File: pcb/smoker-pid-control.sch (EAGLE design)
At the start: 16 parts, among them Q1 IRLIZ44N, SW1 EC12E_SW

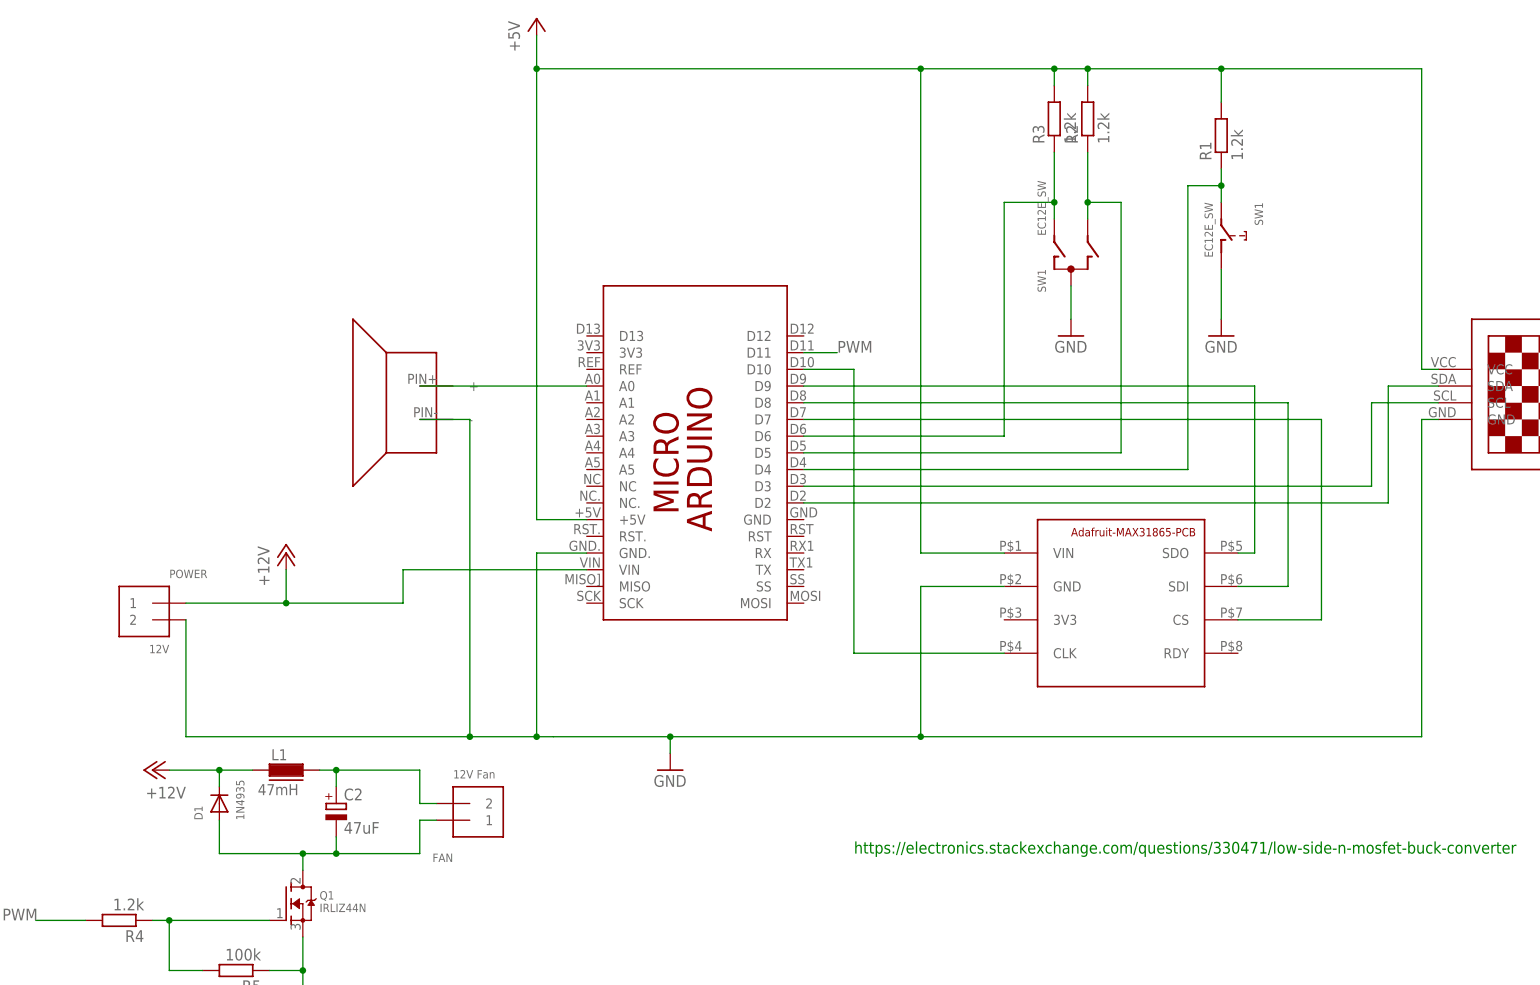
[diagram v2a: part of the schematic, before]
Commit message: single layer Layout, groundplane fix, stronger airwires
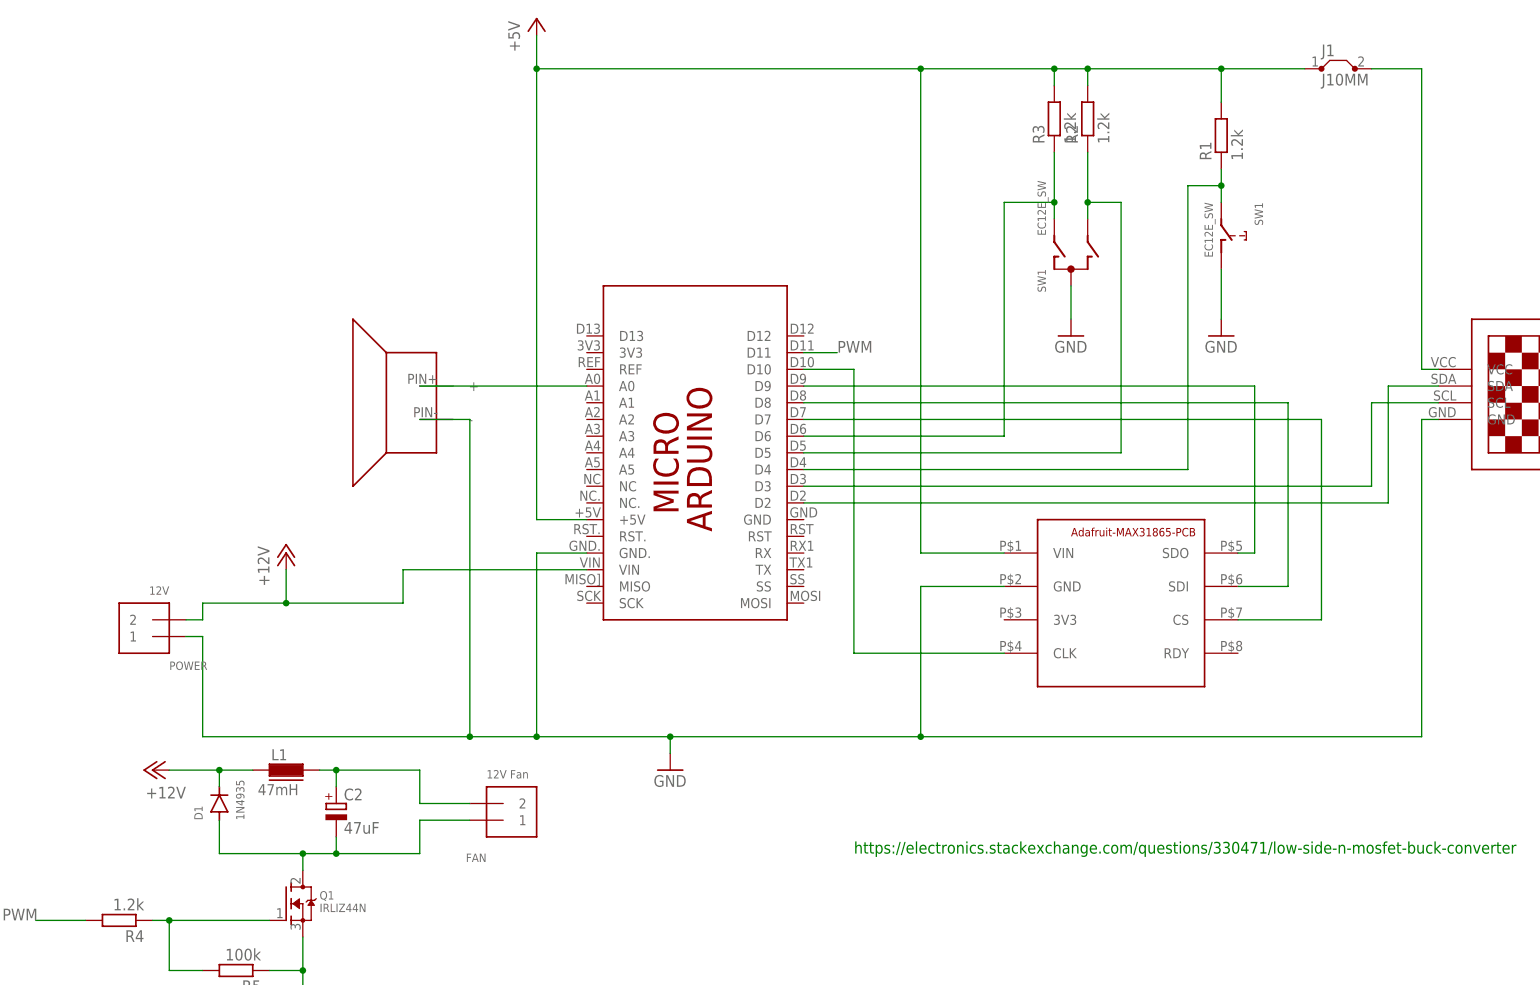
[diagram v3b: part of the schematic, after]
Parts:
- added J1: J10MM, jumper:J10MM
- D1: device adafruit:DIODEDO-1N4148 -> diode:DIODE-DO34-7
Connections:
- new net N$13: J1.2, U$2.VCC
- net +12V: now also POWER.2; no longer POWER.1
- net +5V: now also J1.1; no longer U$2.VCC
- net GND: now also POWER.1; no longer POWER.2
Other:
- moved on the sheet: FAN, POWER
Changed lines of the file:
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@@
 <layers>
 <layer number="1" name="Top" color="4" fill="1" visible="no" active="no"/>
+<layer number="2" name="Route2" color="1" fill="3" visible="no" active="no"/>
+<layer number="3" name="Route3" color="4" fill="3" visible="no" active="no"/>
+<layer number="4" name="Route4" color="1" fill="4" visible="no" active="no"/>
+<layer number="5" name="Route5" color="4" fill="4" visible="no" active="no"/>
+<layer number="6" name="Route6" color="1" fill="8" visible="no" active="no"/>
+<layer number="7" name="Route7" color="4" fill="8" visible="no" active="no"/>
+<layer number="8" name="Route8" color="1" fill="2" visible="no" active="no"/>
+<layer number="9" name="Route9" color="4" fill="2" visible="no" active="no"/>
+<layer number="10" name="Route10" color="1" fill="7" visible="no" active="no"/>
+<layer number="11" name="Route11" color="4" fill="7" visible="no" active="no"/>
+<layer number="12" name="Route12" color="1" fill="5" visible="no" active="no"/>
+<layer number="13" name="Route13" color="4" fill="5" visible="no" active="no"/>
+<layer number="14" name="Route14" color="1" fill="6" visible="no" active="no"/>
+<layer number="15" name="Route15" color="4" fill="6" visible="no" active="no"/>
 <layer number="16" name="Bottom" color="1" fill="1" visible="no" active="no"/>
 <layer number="17" name="Pads" color="2" fill="1" visible="no" active="no"/>
@@
 <part name="Q1" library="adafruit" library_urn="urn:adsk.eagle:library:420" deviceset="MOSFET-N" device="GDS_TO220V" package3d_urn="urn:adsk.eagle:package:6240882/1" value="IRLIZ44N"/>
 <part name="L1" library="_fastron_07HCP" deviceset="07HCP-*" device="" technology="100U" value="47mH"/>
-<part name="D1" library="adafruit" library_urn="urn:adsk.eagle:library:420" deviceset="DIODE" device="DO-1N4148" package3d_urn="urn:adsk.eagle:package:6240748/1" value="1N4935"/>
+<part name="D1" library="diode" library_urn="urn:adsk.eagle:library:210" deviceset="DIODE-" device="DO34-7" package3d_urn="urn:adsk.eagle:package:43348/1" value="1N4935"/>
 <part name="C2" library="rcl" library_urn="urn:adsk.eagle:library:334" deviceset="CPOL-EU" device="E5-8.5" package3d_urn="urn:adsk.eagle:package:23374/1" value="47uF"/>
 <part name="P+3" library="supply1" library_urn="urn:adsk.eagle:library:371" deviceset="+12V" device=""/>
@@
 <part name="R4" library="rcl" library_urn="urn:adsk.eagle:library:334" deviceset="R-EU_" device="0207/10" package3d_urn="urn:adsk.eagle:package:23491/2" value="1.2k"/>
 <part name="R5" library="rcl" library_urn="urn:adsk.eagle:library:334" deviceset="R-EU_" device="0207/10" package3d_urn="urn:adsk.eagle:package:23491/2" value="100k"/>
+<part name="J1" library="jumper" library_urn="urn:adsk.eagle:library:252" deviceset="J" device="10MM" package3d_urn="urn:adsk.eagle:package:15468/1"/>
 </parts>
 <sheets>
@@
 <attribute name="VALUE" x="193.04" y="208.28" size="1.27" layer="96" rot="R270"/>
 </instance>
-<instance part="POWER" gate="G$1" x="33.02" y="144.78" smashed="yes" rot="MR0">
-<attribute name="VALUE" x="35.56" y="139.7" size="1.27" layer="96" rot="MR0"/>
-<attribute name="NAME" x="35.56" y="152.4" size="1.27" layer="95" rot="MR180"/>
-</instance>
-<instance part="FAN" gate="G$1" x="81.28" y="116.84" smashed="yes" rot="MR180">
-<attribute name="VALUE" x="78.74" y="121.92" size="1.27" layer="96" rot="MR180"/>
-<attribute name="NAME" x="78.74" y="109.22" size="1.27" layer="95" rot="R180"/>
+<instance part="POWER" gate="G$1" x="33.02" y="144.78" smashed="yes" rot="R180">
+<attribute name="VALUE" x="35.56" y="149.86" size="1.27" layer="96" rot="R180"/>
+<attribute name="NAME" x="35.56" y="137.16" size="1.27" layer="95"/>
+</instance>
+<instance part="FAN" gate="G$1" x="86.36" y="116.84" smashed="yes" rot="MR180">
+<attribute name="VALUE" x="83.82" y="121.92" size="1.27" layer="96" rot="MR180"/>
+<attribute name="NAME" x="83.82" y="109.22" size="1.27" layer="95" rot="R180"/>
 </instance>
 <instance part="GND1" gate="1" x="111.76" y="121.92" smashed="yes">
@@
 <attribute name="NAME" x="49.53" y="89.9414" size="1.778" layer="95" rot="R180"/>
 <attribute name="VALUE" x="49.53" y="94.742" size="1.778" layer="96" rot="R180"/>
+</instance>
+<instance part="J1" gate="1" x="213.36" y="228.6" smashed="yes">
+<attribute name="NAME" x="210.82" y="230.505" size="1.778" layer="95"/>
+<attribute name="VALUE" x="210.82" y="226.06" size="1.778" layer="96"/>
 </instance>
 </instances>
@@
 <net name="+12V" class="0">
 <segment>
-<pinref part="POWER" gate="G$1" pin="1"/>
-<wire x1="38.1" y1="147.32" x2="53.34" y2="147.32" width="0.1524" layer="91"/>
 <wire x1="53.34" y1="147.32" x2="71.12" y2="147.32" width="0.1524" layer="91"/>
 <wire x1="71.12" y1="147.32" x2="71.12" y2="152.4" width="0.1524" layer="91"/>
@@
 <pinref part="P+1" gate="1" pin="+12V"/>
 <wire x1="53.34" y1="152.4" x2="53.34" y2="147.32" width="0.1524" layer="91"/>
+<pinref part="POWER" gate="G$1" pin="2"/>
+<wire x1="38.1" y1="144.78" x2="40.64" y2="144.78" width="0.1524" layer="91"/>
+<wire x1="40.64" y1="144.78" x2="40.64" y2="147.32" width="0.1524" layer="91"/>
+<wire x1="40.64" y1="147.32" x2="53.34" y2="147.32" width="0.1524" layer="91"/>
 <junction x="53.34" y="147.32"/>
 </segment>
@@
 <segment>
 <wire x1="81.28" y1="127" x2="91.44" y2="127" width="0.1524" layer="91"/>
-<wire x1="93.98" y1="127" x2="111.76" y2="127" width="0.1524" layer="91"/>
+<wire x1="91.44" y1="127" x2="111.76" y2="127" width="0.1524" layer="91"/>
 <wire x1="111.76" y1="127" x2="149.86" y2="127" width="0.1524" layer="91"/>
 <wire x1="149.86" y1="127" x2="226.06" y2="127" width="0.1524" layer="91"/>
@@
 <wire x1="228.6" y1="175.26" x2="226.06" y2="175.26" width="0.1524" layer="91"/>
 <wire x1="226.06" y1="175.26" x2="226.06" y2="127" width="0.1524" layer="91"/>
-<wire x1="38.1" y1="127" x2="81.28" y2="127" width="0.1524" layer="91"/>
-<wire x1="38.1" y1="127" x2="38.1" y2="144.78" width="0.1524" layer="91"/>
-<pinref part="POWER" gate="G$1" pin="2"/>
 <pinref part="GND1" gate="1" pin="GND"/>
+<wire x1="40.64" y1="127" x2="81.28" y2="127" width="0.1524" layer="91"/>
 <wire x1="111.76" y1="124.46" x2="111.76" y2="127" width="0.1524" layer="91"/>
 <junction x="111.76" y="127"/>
@@
 <wire x1="99.06" y1="154.94" x2="91.44" y2="154.94" width="0.1524" layer="91"/>
 <wire x1="91.44" y1="154.94" x2="91.44" y2="127" width="0.1524" layer="91"/>
-<wire x1="91.44" y1="127" x2="93.98" y2="127" width="0.1524" layer="91"/>
 <junction x="91.44" y="127"/>
+<pinref part="POWER" gate="G$1" pin="1"/>
+<wire x1="38.1" y1="142.24" x2="40.64" y2="142.24" width="0.1524" layer="91"/>
+<wire x1="40.64" y1="142.24" x2="40.64" y2="127" width="0.1524" layer="91"/>
 </segment>
 <segment>
@@
 <wire x1="170.18" y1="228.6" x2="175.26" y2="228.6" width="0.1524" layer="91"/>
 <wire x1="175.26" y1="228.6" x2="195.58" y2="228.6" width="0.1524" layer="91"/>
-<wire x1="195.58" y1="228.6" x2="226.06" y2="228.6" width="0.1524" layer="91"/>
-<wire x1="226.06" y1="228.6" x2="226.06" y2="182.88" width="0.1524" layer="91"/>
-<pinref part="U$2" gate="G$1" pin="VCC"/>
-<wire x1="226.06" y1="182.88" x2="228.6" y2="182.88" width="0.1524" layer="91"/>
 <pinref part="U$1" gate="G$1" pin="VIN"/>
 <wire x1="162.56" y1="154.94" x2="149.86" y2="154.94" width="0.1524" layer="91"/>
@@
 <pinref part="R1" gate="G$1" pin="2"/>
 <wire x1="195.58" y1="223.52" x2="195.58" y2="228.6" width="0.1524" layer="91"/>
-<junction x="195.58" y="228.6"/>
 <pinref part="R2" gate="G$1" pin="2"/>
 <wire x1="175.26" y1="226.06" x2="175.26" y2="228.6" width="0.1524" layer="91"/>
@@
 <wire x1="170.18" y1="226.06" x2="170.18" y2="228.6" width="0.1524" layer="91"/>
 <junction x="170.18" y="228.6"/>
+<pinref part="J1" gate="1" pin="1"/>
+<wire x1="208.28" y1="228.6" x2="195.58" y2="228.6" width="0.1524" layer="91"/>
+<junction x="195.58" y="228.6"/>
 </segment>
 </net>
@@
 <wire x1="73.66" y1="121.92" x2="73.66" y2="116.84" width="0.1524" layer="91"/>
 <pinref part="FAN" gate="G$1" pin="2"/>
-<wire x1="73.66" y1="116.84" x2="76.2" y2="116.84" width="0.1524" layer="91"/>
+<wire x1="73.66" y1="116.84" x2="81.28" y2="116.84" width="0.1524" layer="91"/>
 </segment>
 </net>
@@
 <segment>
 <pinref part="D1" gate="G$1" pin="A"/>
-<pinref part="FAN" gate="G$1" pin="1"/>
 <wire x1="43.18" y1="109.22" x2="43.18" y2="114.3" width="0.1524" layer="91"/>
-<wire x1="76.2" y1="114.3" x2="73.66" y2="114.3" width="0.1524" layer="91"/>
 <wire x1="73.66" y1="114.3" x2="73.66" y2="109.22" width="0.1524" layer="91"/>
 <wire x1="73.66" y1="109.22" x2="60.96" y2="109.22" width="0.1524" layer="91"/>
@@
 <wire x1="55.88" y1="106.68" x2="55.88" y2="109.22" width="0.1524" layer="91"/>
 <junction x="55.88" y="109.22"/>
+<pinref part="FAN" gate="G$1" pin="1"/>
+<wire x1="81.28" y1="114.3" x2="73.66" y2="114.3" width="0.1524" layer="91"/>
 </segment>
 </net>
@@
 </segment>
 </net>
+<net name="N$13" class="0">
+<segment>
+<pinref part="U$2" gate="G$1" pin="VCC"/>
+<wire x1="226.06" y1="228.6" x2="226.06" y2="182.88" width="0.1524" layer="91"/>
+<wire x1="226.06" y1="182.88" x2="228.6" y2="182.88" width="0.1524" layer="91"/>
+<pinref part="J1" gate="1" pin="2"/>
+<wire x1="218.44" y1="228.6" x2="226.06" y2="228.6" width="0.1524" layer="91"/>
+</segment>
+</net>

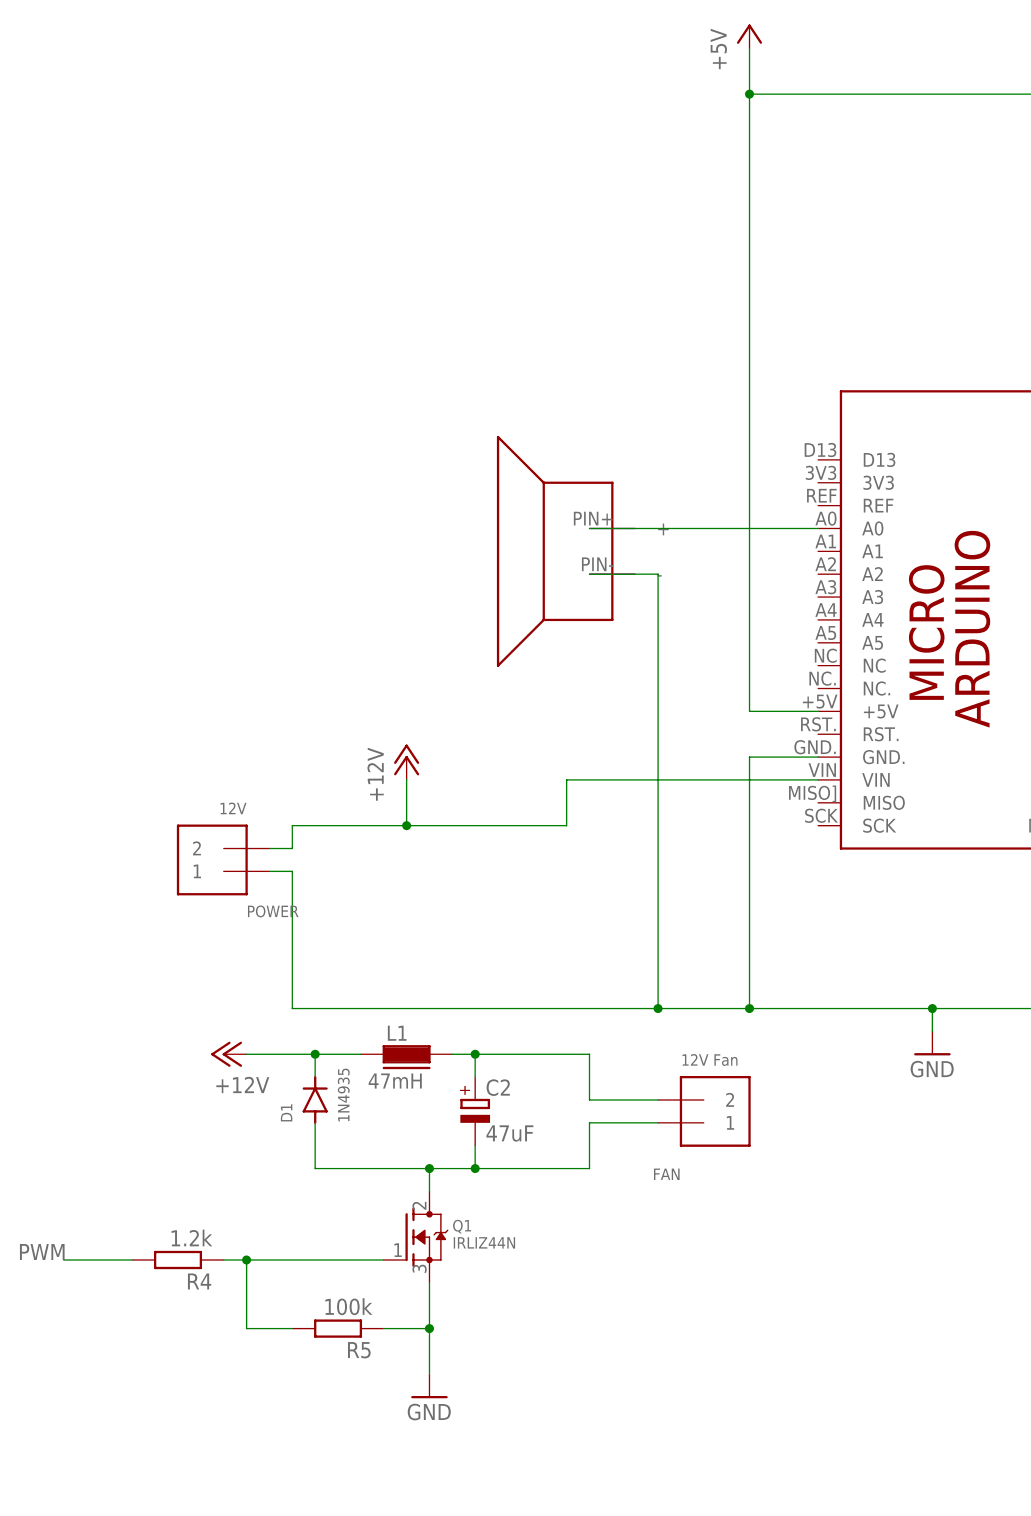
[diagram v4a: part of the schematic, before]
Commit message: fix Micro power path from Vin to 5V pin, separate 5V and 12V supply
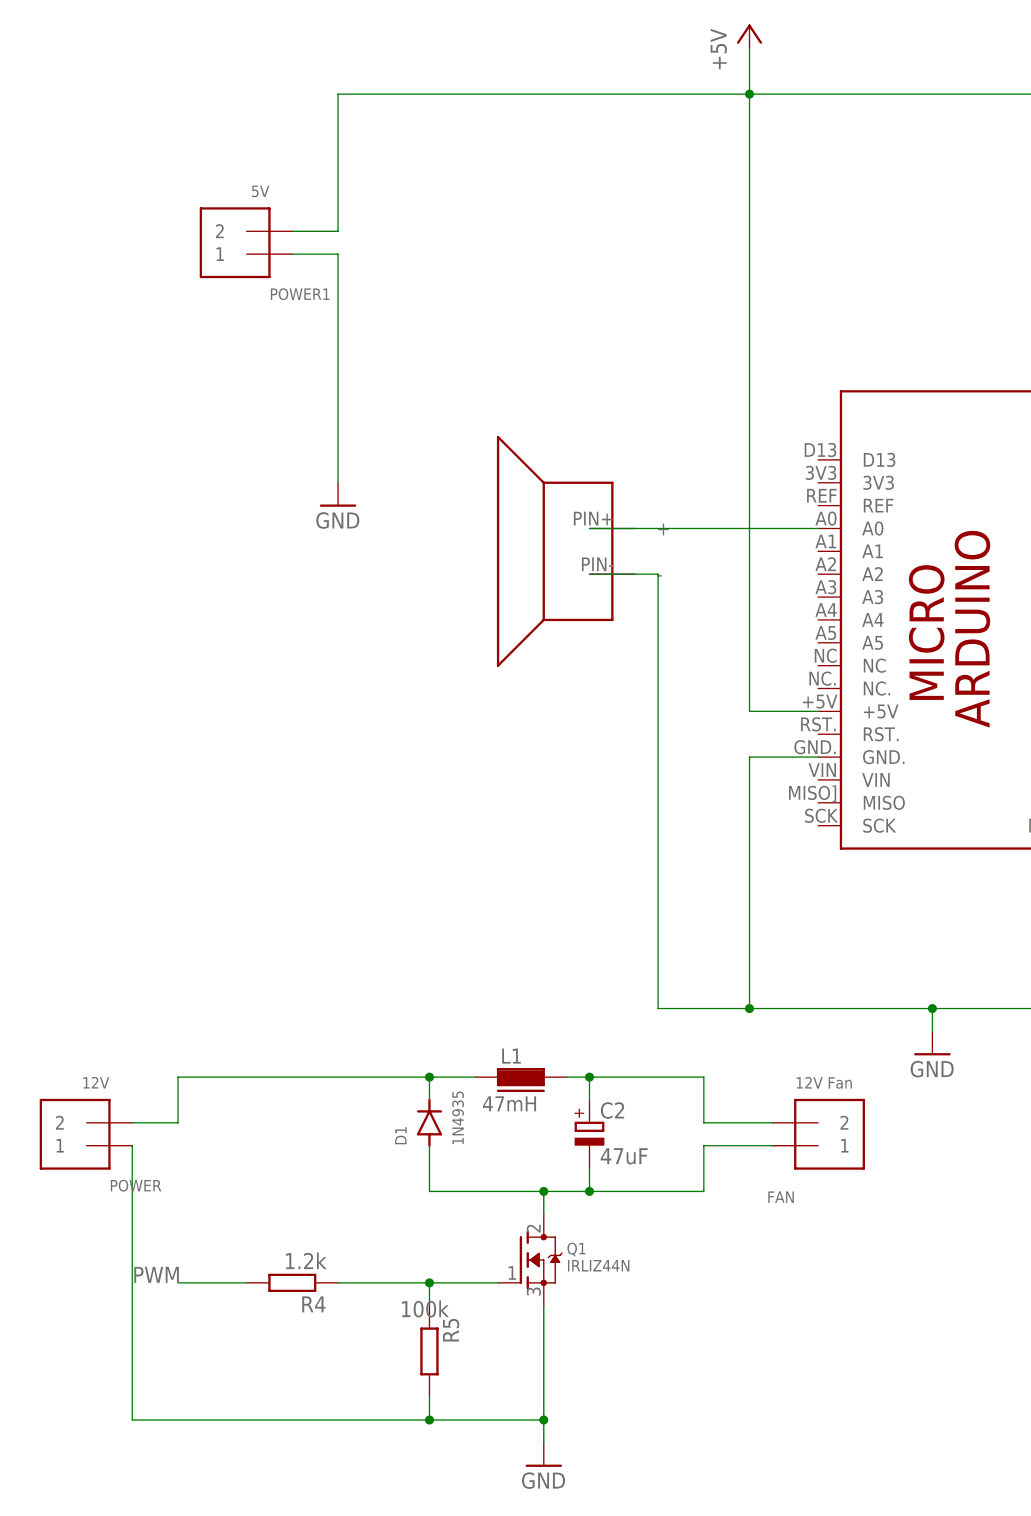
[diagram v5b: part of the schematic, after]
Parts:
- added POWER1: 5V, smoker-pid-control:TERMBLOCK_1X2
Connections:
- removed net +12V: D1.C, L1.1, PCB1.VIN, POWER.2
- new net N$15: D1.C, L1.1, POWER.2
- net +5V: now also POWER1.2
- net GND: now also POWER1.1, R5.2; no longer R5.1
- net N$12: now also R5.1; no longer R5.2
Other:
- moved on the sheet: C2, D1, FAN, L1, POWER, Q1, R4, R5
